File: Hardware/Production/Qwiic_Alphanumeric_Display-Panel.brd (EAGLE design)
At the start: 40.6 x 30.5 mm, 32 parts, among them J1 PTH, J2 Qwiic Right Angle, U2 HT16K33

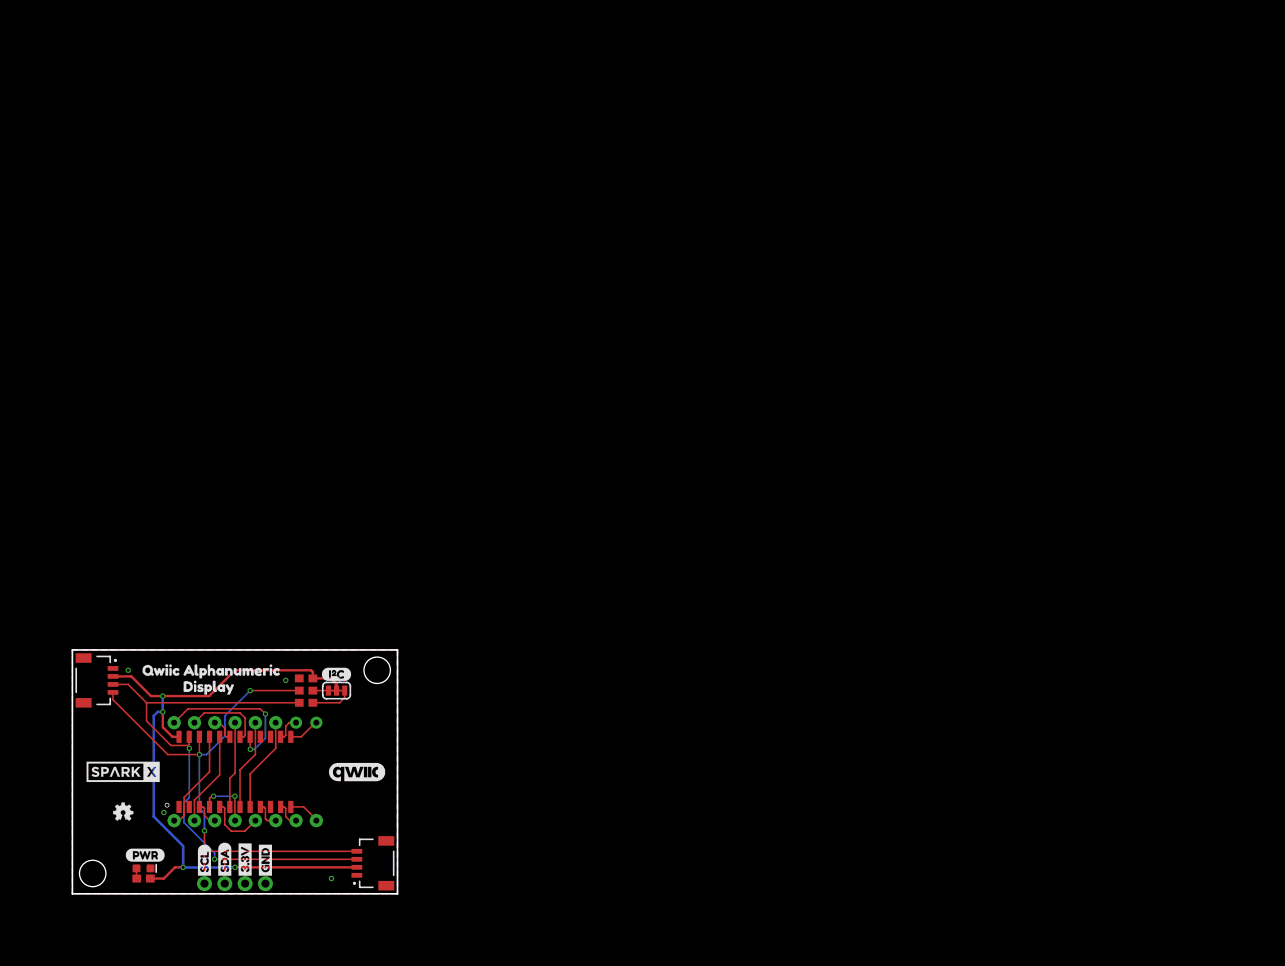
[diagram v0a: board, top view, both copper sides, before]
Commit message: Added Panelized Board and Gerber Files
Updated the HT16K33 Footprint, fixed the board files to match the footprint, added the panelized production board and gerber files for ordering the board
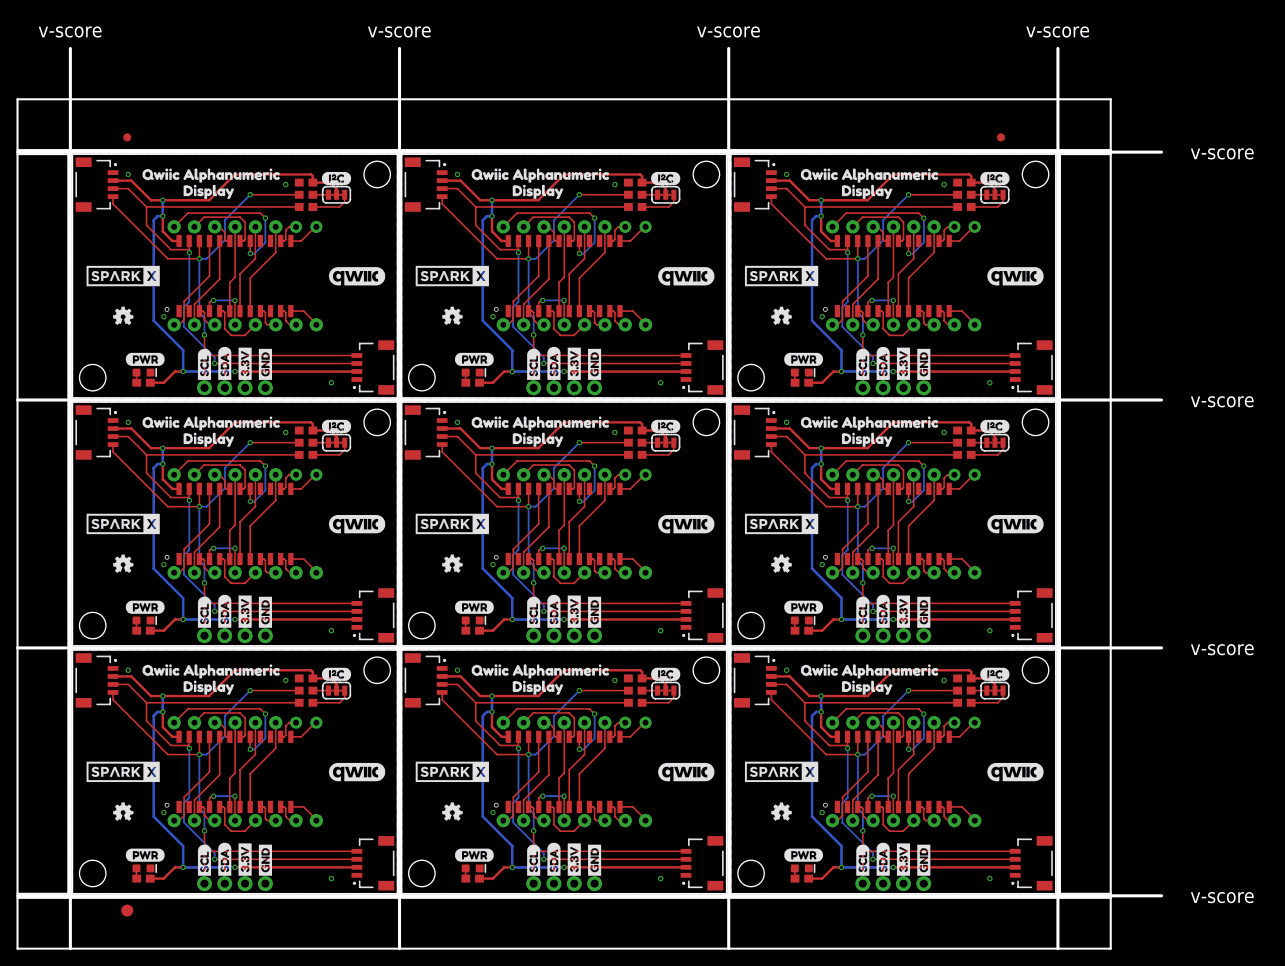
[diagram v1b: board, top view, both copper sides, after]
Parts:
- removed FRAME1: FRAME-LETTER, SparkFun-Aesthetics:CREATIVE_COMMONS
- added C2, C3, C4, C5, C6, C7, C8, C9: 0.1uF, SparkFun-Capacitors:0603
- added D2, D3, D4, D5, D6, D7, D8, D9: RED, SparkFun-LED:LED-0603
- added E$1, E$2: (no value), SparkFun-Aesthetics:FIDUCIAL-1X2
- added E$3: (no value), SparkFun-Retired:FIDUCIAL-1.5X3
- added I2C1, I2C2, I2C3, I2C4, I2C5, I2C6, I2C7, I2C8: JUMPER-SMT_3_2-NC_TRACE_SILK, SparkFun-Jumpers:SMT-JUMPER_3_2-NC_TRACE_SILK
- added J10, J13, J16, J19, J22, J25, J4, J7: PTH, SparkFun-Connectors:JST04_1MM_RA
- added J11, J14, J17, J20, J23, J26, J5, J8: Qwiic Right Angle, SparkFun-Connectors:JST04_1MM_RA
- added J12, J15, J18, J21, J24, J27, J6, J9: (no value), SparkFun-Connectors:1X04_NO_SILK
- added JP10, JP11, JP12, JP13, JP14, JP15, JP16, JP17, JP18, JP2, JP3, JP4, JP5, JP6, JP7, JP9: STAND-OFF, SparkFun:STAND-OFF
- added LOGO2, LOGO3, LOGO4, LOGO5, LOGO6, LOGO7, LOGO8, LOGO9: OSHW-LOGOMINI, SparkFun-Aesthetics:OSHW-LOGO-MINI
- added R10, R13, R16, R19, R2, R22, R25, R7: 1k, SparkFun-Resistors:0603
- added R11, R12, R14, R15, R17, R18, R20, R21, R23, R24, R26, R27, R3, R6, R8, R9: 2.2k, SparkFun-Resistors:0603
- added U$100, U$102, U$117, U$119, U$134, U$136, U$151, U$153, U$32, U$34, U$49, U$51, U$66, U$68, U$83, U$85: (no value), buzzard_labels (4):DISPLAY1
- added U$101, U$116, U$118, U$133, U$135, U$150, U$152, U$31, U$33, U$48, U$50, U$65, U$67, U$82, U$84, U$99: (no value), buzzard_labels (4):QWIIC_ALPHANUMERIC0
- added U$103, U$108, U$120, U$125, U$137, U$142, U$18, U$23, U$35, U$40, U$52, U$57, U$69, U$74, U$86, U$91: (no value), buzzard_labels:3#3V1
- added U$104, U$109, U$121, U$126, U$138, U$143, U$19, U$24, U$36, U$41, U$53, U$58, U$70, U$75, U$87, U$92: (no value), buzzard_labels:GND0
- added U$105, U$122, U$139, U$20, U$37, U$54, U$71, U$88: (no value), buzzard_labels:PWR5
- added U$106, U$110, U$123, U$127, U$140, U$144, U$21, U$25, U$38, U$42, U$55, U$59, U$72, U$76, U$89, U$93: (no value), buzzard_labels:SCL3
- added U$107, U$111, U$124, U$128, U$141, U$145, U$22, U$26, U$39, U$43, U$56, U$60, U$73, U$77, U$90, U$94: (no value), buzzard_labels:SDA2
- added U$112, U$129, U$146, U$27, U$44, U$61, U$78, U$95: (no value), Labels:I_SUPER2_C-()-04
- added U$113, U$130, U$147, U$28, U$45, U$62, U$79, U$96: (no value), Labels:QWIIC_COPYRIGHT_MEDIUM
- added U$114, U$115, U$131, U$132, U$148, U$149, U$29, U$30, U$46, U$47, U$63, U$64, U$80, U$81, U$97, U$98: (no value), SparkX:SPARKX-MEDIUM
- added U10, U12, U14, U16, U18, U4, U6, U8: HT16K33, Alphanumeric_Display_Library:HT16K33
- added U11, U13, U15, U17, U3, U5, U7, U9: (no value), Alphanumeric_Display_Library:SILSMART_DISPLAY
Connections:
- new net 3.3V1: C2.1, I2C1.2, J4.2, J5.2, J6.2, R2.2, U4.24
- new net 3.3V2: C3.1, I2C2.2, J7.2, J8.2, J9.2, R7.2, U6.24
- new net 3.3V3: C4.1, I2C3.2, J10.2, J11.2, J12.2, R10.2, U8.24
- new net 3.3V4: C5.1, I2C4.2, J13.2, J14.2, J15.2, R13.2, U10.24
- new net 3.3V5: C6.1, I2C5.2, J16.2, J17.2, J18.2, R16.2, U12.24
- new net 3.3V6: C7.1, I2C6.2, J19.2, J20.2, J21.2, R19.2, U14.24
- new net 3.3V7: C8.1, I2C7.2, J22.2, J23.2, J24.2, R22.2, U16.24
- new net 3.3V8: C9.1, I2C8.2, J25.2, J26.2, J27.2, R25.2, U18.24
- new net COM_A1: U3.14, U4.8
- new net COM_A2: U5.14, U6.8
- new net COM_A3: U7.14, U8.8
- new net COM_A4: U10.8, U9.14
- new net COM_A5: U11.14, U12.8
- new net COM_A6: U13.14, U14.8
- new net COM_A7: U15.14, U16.8
- new net COM_A8: U17.14, U18.8
- new net COM_B1: U3.13, U4.7
- new net COM_B2: U5.13, U6.7
- new net COM_B3: U7.13, U8.7
- new net COM_B4: U10.7, U9.13
- new net COM_B5: U11.13, U12.7
- new net COM_B6: U13.13, U14.7
- new net COM_B7: U15.13, U16.7
- new net COM_B8: U17.13, U18.7
- new net COM_C1: U3.4, U4.5
- new net COM_C2: U5.4, U6.5
- new net COM_C3: U7.4, U8.5
- new net COM_C4: U10.5, U9.4
- new net COM_C5: U11.4, U12.5
- new net COM_C6: U13.4, U14.5
- new net COM_C7: U15.4, U16.5
- new net COM_C8: U17.4, U18.5
- new net COM_D1: U3.3, U4.9
- new net COM_D2: U5.3, U6.9
- new net COM_D3: U7.3, U8.9
- new net COM_D4: U10.9, U9.3
- new net COM_D5: U11.3, U12.9
- new net COM_D6: U13.3, U14.9
- new net COM_D7: U15.3, U16.9
- new net COM_D8: U17.3, U18.9
- new net COM_E1: U3.6, U4.3
- new net COM_E2: U5.6, U6.3
- new net COM_E3: U7.6, U8.3
- new net COM_E4: U10.3, U9.6
- new net COM_E5: U11.6, U12.3
- new net COM_E6: U13.6, U14.3
- new net COM_E7: U15.6, U16.3
- new net COM_E8: U17.6, U18.3
- new net COM_F1: U3.12, U4.6
- new net COM_F2: U5.12, U6.6
- new net COM_F3: U7.12, U8.6
- new net COM_F4: U10.6, U9.12
- new net COM_F5: U11.12, U12.6
- new net COM_F6: U13.12, U14.6
- new net COM_F7: U15.12, U16.6
- new net COM_F8: U17.12, U18.6
- new net COM_G2: U3.5, U4.4
- new net COM_G3: U5.5, U6.4
- new net COM_G4: U7.5, U8.4
- new net COM_G5: U10.4, U9.5
- new net COM_G6: U11.5, U12.4
- new net COM_G7: U13.5, U14.4
- new net COM_G8: U15.5, U16.4
- new net COM_G9: U17.5, U18.4
- new net DIG_1A1: U3.16, U4.13
- new net DIG_1A2: U5.16, U6.13
- new net DIG_1A3: U7.16, U8.13
- new net DIG_1A4: U10.13, U9.16
- new net DIG_1A5: U11.16, U12.13
- new net DIG_1A6: U13.16, U14.13
- new net DIG_1A7: U15.16, U16.13
- new net DIG_1A8: U17.16, U18.13
- new net DIG_1B1: U3.1, U4.12
- new net DIG_1B2: U5.1, U6.12
- new net DIG_1B3: U7.1, U8.12
- new net DIG_1B4: U10.12, U9.1
- new net DIG_1B5: U11.1, U12.12
- new net DIG_1B6: U13.1, U14.12
- new net DIG_1B7: U15.1, U16.12
- new net DIG_1B8: U17.1, U18.12
- new net DIG_2A1: U3.15, U4.14
- new net DIG_2A2: U5.15, U6.14
- new net DIG_2A3: U7.15, U8.14
- new net DIG_2A4: U10.14, U9.15
- new net DIG_2A5: U11.15, U12.14
- new net DIG_2A6: U13.15, U14.14
- new net DIG_2A7: U15.15, U16.14
- new net DIG_2A8: U17.15, U18.14
- new net DIG_2B1: U3.2, U4.11
- new net DIG_2B2: U5.2, U6.11
- new net DIG_2B3: U7.2, U8.11
- new net DIG_2B4: U10.11, U9.2
- new net DIG_2B5: U11.2, U12.11
- new net DIG_2B6: U13.2, U14.11
- new net DIG_2B7: U15.2, U16.11
- new net DIG_2B8: U17.2, U18.11
- new net DIG_3A1: U3.11, U4.19
- new net DIG_3A2: U5.11, U6.19
- new net DIG_3A3: U7.11, U8.19
- new net DIG_3A4: U10.19, U9.11
- new net DIG_3A5: U11.11, U12.19
- new net DIG_3A6: U13.11, U14.19
- new net DIG_3A7: U15.11, U16.19
- new net DIG_3A8: U17.11, U18.19
- new net DIG_3B1: U3.10, U4.18
- new net DIG_3B2: U5.10, U6.18
- new net DIG_3B3: U7.10, U8.18
- new net DIG_3B4: U10.18, U9.10
- new net DIG_3B5: U11.10, U12.18
- new net DIG_3B6: U13.10, U14.18
- new net DIG_3B7: U15.10, U16.18
- new net DIG_3B8: U17.10, U18.18
- new net DIG_4A1: U3.8, U4.21
- new net DIG_4A2: U5.8, U6.21
- new net DIG_4A3: U7.8, U8.21
- new net DIG_4A4: U10.21, U9.8
- new net DIG_4A5: U11.8, U12.21
- new net DIG_4A6: U13.8, U14.21
- new net DIG_4A7: U15.8, U16.21
- new net DIG_4A8: U17.8, U18.21
- new net DIG_4B1: U3.9, U4.17
- new net DIG_4B2: U5.9, U6.17
- new net DIG_4B3: U7.9, U8.17
- new net DIG_4B4: U10.17, U9.9
- new net DIG_4B5: U11.9, U12.17
- new net DIG_4B6: U13.9, U14.17
- new net DIG_4B7: U15.9, U16.17
- new net DIG_4B8: U17.9, U18.17
- new net DIG_DP1: U3.7, U4.20
- new net DIG_DP2: U5.7, U6.20
- new net DIG_DP3: U7.7, U8.20
- new net DIG_DP4: U10.20, U9.7
- new net DIG_DP5: U11.7, U12.20
- new net DIG_DP6: U13.7, U14.20
- new net DIG_DP7: U15.7, U16.20
- new net DIG_DP8: U17.7, U18.20
- new net GND1: C2.2, D2.C, J4.1, J5.1, J6.1, U4.1
- new net GND2: C3.2, D3.C, J7.1, J8.1, J9.1, U6.1
- new net GND3: C4.2, D4.C, J10.1, J11.1, J12.1, U8.1
- new net GND4: C5.2, D5.C, J13.1, J14.1, J15.1, U10.1
- new net GND5: C6.2, D6.C, J16.1, J17.1, J18.1, U12.1
- new net GND6: C7.2, D7.C, J19.1, J20.1, J21.1, U14.1
- new net GND7: C8.2, D8.C, J22.1, J23.1, J24.1, U16.1
- new net GND8: C9.2, D9.C, J25.1, J26.1, J27.1, U18.1
- new net N$10: D4.A, R10.1
- new net N$11: I2C3.1, R12.2
- new net N$12: I2C3.3, R11.2
- new net N$13: D5.A, R13.1
- new net N$14: I2C4.1, R15.2
- new net N$15: I2C4.3, R14.2
- new net N$16: D6.A, R16.1
- new net N$17: I2C5.1, R18.2
- new net N$18: I2C5.3, R17.2
- new net N$19: D7.A, R19.1
- new net N$2: D2.A, R2.1
- new net N$20: I2C6.1, R21.2
- new net N$21: I2C6.3, R20.2
- new net N$22: D8.A, R22.1
- new net N$23: I2C7.1, R24.2
- new net N$24: I2C7.3, R23.2
- new net N$25: D9.A, R25.1
- new net N$26: I2C8.1, R27.2
- new net N$27: I2C8.3, R26.2
- new net N$3: I2C1.1, R6.2
- new net N$6: I2C1.3, R3.2
- new net N$7: D3.A, R7.1
- new net N$8: I2C2.1, R9.2
- new net N$9: I2C2.3, R8.2
- new net SCL1: J4.4, J5.4, J6.4, R6.1, U4.22
- new net SCL2: J7.4, J8.4, J9.4, R9.1, U6.22
- new net SCL3: J10.4, J11.4, J12.4, R12.1, U8.22
- new net SCL4: J13.4, J14.4, J15.4, R15.1, U10.22
- new net SCL5: J16.4, J17.4, J18.4, R18.1, U12.22
- new net SCL6: J19.4, J20.4, J21.4, R21.1, U14.22
- new net SCL7: J22.4, J23.4, J24.4, R24.1, U16.22
- new net SCL8: J25.4, J26.4, J27.4, R27.1, U18.22
- new net SDA1: J4.3, J5.3, J6.3, R3.1, U4.23
- new net SDA2: J7.3, J8.3, J9.3, R8.1, U6.23
- new net SDA3: J10.3, J11.3, J12.3, R11.1, U8.23
- new net SDA4: J13.3, J14.3, J15.3, R14.1, U10.23
- new net SDA5: J16.3, J17.3, J18.3, R17.1, U12.23
- new net SDA6: J19.3, J20.3, J21.3, R20.1, U14.23
- new net SDA7: J22.3, J23.3, J24.3, R23.1, U16.23
- new net SDA8: J25.3, J26.3, J27.3, R26.1, U18.23
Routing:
- net 3.3V6: track 0.00 -> 88.9 mm, vias 0 -> 4
- net 3.3V3: track 0.00 -> 88.9 mm, vias 0 -> 4
- net 3.3V8: track 0.00 -> 88.9 mm, vias 0 -> 4
- net 3.3V7: track 0.00 -> 88.9 mm, vias 0 -> 4
- net 3.3V5: track 0.00 -> 88.9 mm, vias 0 -> 4
- net 3.3V4: track 0.00 -> 88.9 mm, vias 0 -> 4
- net 3.3V2: track 0.00 -> 88.9 mm, vias 0 -> 4
- net 3.3V1: track 0.00 -> 88.9 mm, vias 0 -> 4
- net SDA8: track 0.00 -> 71.1 mm, vias 0 -> 2
- net SDA2: track 0.00 -> 71.1 mm, vias 0 -> 2
- net SDA1: track 0.00 -> 71.1 mm, vias 0 -> 2
- net SDA7: track 0.00 -> 71.1 mm, vias 0 -> 2
- net SDA6: track 0.00 -> 71.1 mm, vias 0 -> 2
- net SDA5: track 0.00 -> 71.1 mm, vias 0 -> 2
- net SDA4: track 0.00 -> 71.1 mm, vias 0 -> 2
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- added copper zone on layer 1, net GND1
- added copper zone on layer 16, net GND1
- added copper zone on layer 1, net GND2
- added copper zone on layer 16, net GND2
- added copper zone on layer 1, net GND3
- added copper zone on layer 16, net GND3
- added copper zone on layer 1, net GND4
- added copper zone on layer 16, net GND4
- added copper zone on layer 1, net GND5
- added copper zone on layer 16, net GND5
- added copper zone on layer 1, net GND6
- added copper zone on layer 16, net GND6
- added copper zone on layer 1, net GND7
- added copper zone on layer 16, net GND7
- added copper zone on layer 1, net GND8
- added copper zone on layer 16, net GND8
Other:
- board size 40.6 x 30.5 mm -> 143 x 112.5 mm
- board text added: "v-score"
- board text removed: "I2C"
- board text removed: "Madison Chodikov"
- board text removed: "U1"

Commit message: Rev X02 ordered!
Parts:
- added 3V1, 3V10, 3V11, 3V12, 3V13, 3V14, 3V15, 3V16, 3V17, 3V18, 3V19, 3V2, 3V20, 3V21, 3V22, 3V23, 3V24, 3V25, 3V3, 3V4, 3V5, 3V6, 3V7, 3V8, 3V9: JUMPER-SMT_2_NC_TRACE_SILK, SparkFun-Jumpers:SMT-JUMPER_2_NC_TRACE_SILK
- added C10, C11, C12, C13, C14, C15, C16, C17, C18, C19, C20, C21, C22, C23, C24, C25: 0.1uF, SparkFun-Capacitors:0603
- added D10, D12, D14, D16, D18, D20, D22, D24, D26, D28, D30, D32, D34, D36, D38, D40, D42, D44, D46, D48, D50: 250mA/100V, SparkFun-DiscreteSemi:SOD-323
- added D11, D13, D15, D17, D19, D21, D23, D25, D27, D29, D31, D33, D35, D37, D39, D41, D43, D45, D47, D49: RED, SparkFun-LED:LED-0603
- added FD1, FD10, FD100, FD11, FD12, FD13, FD14, FD15, FD16, FD17, FD18, FD19, FD2, FD20, FD21, FD22, FD23, FD24, FD25, FD26, FD27, FD28, FD29, FD3, FD30, FD31, FD32, FD33, FD34, FD35, FD36, FD37, FD38, FD39, FD4, FD40, FD41, FD42, FD43, FD44, FD45, FD46, FD47, FD48, FD49, FD5, FD50, FD51, FD52, FD53, FD54, FD55, FD56, FD57, FD58, FD59, FD6, FD60, FD61, FD62, FD63, FD64, FD65, FD66, FD67, FD68, FD69, FD7, FD70, FD71, FD72, FD73, FD74, FD75, FD76, FD77, FD78, FD79, FD8, FD80, FD81, FD82, FD83, FD84, FD85, FD86, FD87, FD88, FD89, FD9, FD90, FD91, FD92, FD93, FD94, FD95, FD96, FD97, FD98, FD99: FIDUCIAL1X2, SparkFun-Aesthetics:FIDUCIAL-1X2
- added H1, H10, H100, H11, H12, H13, H14, H15, H16, H17, H18, H19, H2, H20, H21, H22, H23, H24, H25, H26, H27, H28, H29, H3, H30, H31, H32, H33, H34, H35, H36, H37, H38, H39, H4, H40, H41, H42, H43, H44, H45, H46, H47, H48, H49, H5, H50, H51, H52, H53, H54, H55, H56, H57, H58, H59, H6, H60, H61, H62, H63, H64, H65, H66, H67, H68, H69, H7, H70, H71, H72, H73, H74, H75, H76, H77, H78, H79, H8, H80, H81, H82, H83, H84, H85, H86, H87, H88, H89, H9, H90, H91, H92, H93, H94, H95, H96, H97, H98, H99: STAND-OFF, SparkFun-Hardware:STAND-OFF
- added I2C10, I2C11, I2C12, I2C13, I2C14, I2C15, I2C16, I2C17, I2C18, I2C19, I2C20, I2C21, I2C22, I2C23, I2C24, I2C9: JUMPER-SMT_3_2-NC_TRACE_SILK, SparkFun-Jumpers:SMT-JUMPER_3_2-NC_TRACE_SILK
- added IC1, IC10, IC11, IC12, IC13, IC14, IC15, IC16, IC17, IC18, IC19, IC2, IC20, IC21, IC22, IC23, IC24, IC25, IC3, IC4, IC5, IC6, IC7, IC8, IC9: (no value), Alphanumeric_Display_Library:HT16K33
- added J28, J31, J34, J37, J40, J43, J46, J49, J52, J55, J58, J61, J64, J67, J70, J73: (no value), SparkFun-Connectors:1X04_NO_SILK
- added J29, J30, J32, J33, J35, J36, J38, J39, J41, J42, J44, J45, J47, J48, J50, J51, J53, J54, J56, J57, J59, J60, J62, J63, J65, J66, J68, J69, J71, J72, J74, J75: Vertical Qwiic Connector, SparkFun-Connectors:JST04_1MM_VERT
- added JP19, JP20, JP21, JP22, JP23, JP24, JP25, JP26, JP27, JP28, JP29, JP30, JP31, JP32, JP33, JP34, JP35, JP36, JP37, JP38, JP39, JP40, JP41, JP42, JP43, JP44, JP45, JP46, JP47, JP48, JP49, JP50: JUMPER-SMT_2_NO_SILK, SparkFun-Jumpers:SMT-JUMPER_2_NO_SILK
- added LOGO10, LOGO11, LOGO12, LOGO13, LOGO14, LOGO15, LOGO16, LOGO17, LOGO18, LOGO19, LOGO20, LOGO21, LOGO22, LOGO23, LOGO24, LOGO25: OSHW-LOGOMINI, SparkFun-Aesthetics:OSHW-LOGO-MINI
- added R100, R104, R105, R109, R110, R114, R115, R119, R120, R124, R125, R29, R30, R34, R35, R39, R40, R44, R45, R49, R50, R54, R55, R59, R60, R64, R65, R69, R70, R74, R75, R79, R80, R84, R85, R89, R90, R94, R95, R99: 39k, SparkFun-Resistors:0603
- added R101, R106, R111, R116, R121, R31, R36, R41, R46, R51, R56, R61, R66, R71, R76, R81, R86, R91, R96: 1k, SparkFun-Resistors:0603
- added R102, R103, R107, R108, R112, R113, R117, R118, R122, R123, R28, R32, R33, R37, R38, R42, R43, R47, R48, R52, R53, R57, R58, R62, R63, R67, R68, R72, R73, R77, R78, R82, R83, R87, R88, R92, R93, R97, R98: 2.2k, SparkFun-Resistors:0603
- added U$154, U$171, U$188, U$205, U$222, U$239, U$256, U$273, U$290, U$307, U$324, U$341, U$358, U$375, U$392, U$409: (no value), buzzard_labels:PWR5
- added U$155, U$172, U$189, U$206, U$223, U$240, U$257, U$274, U$291, U$308, U$325, U$342, U$359, U$376, U$393, U$410: (no value), Labels:I_SUPER2_C-()-04
- added U$156, U$158, U$173, U$175, U$190, U$192, U$207, U$209, U$224, U$226, U$241, U$243, U$258, U$260, U$275, U$277, U$292, U$294, U$309, U$311, U$326, U$328, U$343, U$345, U$360, U$362, U$377, U$379, U$394, U$396, U$411, U$413: (no value), buzzard_labels (4):QWIIC_ALPHANUMERIC0
- added U$157, U$159, U$174, U$176, U$191, U$193, U$208, U$210, U$225, U$227, U$242, U$244, U$259, U$261, U$276, U$278, U$293, U$295, U$310, U$312, U$327, U$329, U$344, U$346, U$361, U$363, U$378, U$380, U$395, U$397, U$412, U$414: (no value), buzzard_labels (4):DISPLAY1
- added U$160, U$161, U$177, U$178, U$194, U$195, U$211, U$212, U$228, U$229, U$245, U$246, U$262, U$263, U$279, U$280, U$296, U$297, U$313, U$314, U$330, U$331, U$347, U$348, U$364, U$365, U$381, U$382, U$398, U$399, U$415, U$416: MOUNTING_HOLE_M2-0.4X6, Alphanumeric_Display_Library:MOUNTING_HOLE_M2-0.4X6
- added U$162, U$179, U$196, U$213, U$230, U$247, U$264, U$281, U$298, U$315, U$332, U$349, U$366, U$383, U$400, U$417: (no value), buzzard_labels (63):A00
- added U$163, U$180, U$197, U$214, U$231, U$248, U$265, U$282, U$299, U$316, U$333, U$350, U$367, U$384, U$401, U$418: (no value), buzzard_labels (63):A11
- added U$164, U$181, U$198, U$215, U$232, U$249, U$266, U$283, U$300, U$317, U$334, U$351, U$368, U$385, U$402, U$419: (no value), SparkFun-Aesthetics:QWIIC_4MM
- added U$165, U$182, U$199, U$216, U$233, U$250, U$267, U$284, U$301, U$318, U$335, U$352, U$369, U$386, U$403, U$420: (no value), buzzard_labels (65):32
- added U$166, U$183, U$200, U$217, U$234, U$251, U$268, U$285, U$302, U$319, U$336, U$353, U$370, U$387, U$404, U$421: (no value), buzzard_labels (65):C0
- added U$167, U$184, U$201, U$218, U$235, U$252, U$269, U$286, U$303, U$320, U$337, U$354, U$371, U$388, U$405, U$422: (no value), buzzard_labels (65):D1
- added U$168, U$185, U$202, U$219, U$236, U$253, U$270, U$287, U$304, U$321, U$338, U$355, U$372, U$389, U$406, U$423: (no value), buzzard_labels (65):G3
- added U$169, U$170, U$186, U$187, U$203, U$204, U$220, U$221, U$237, U$238, U$254, U$255, U$271, U$272, U$288, U$289, U$305, U$306, U$322, U$323, U$339, U$340, U$356, U$357, U$373, U$374, U$390, U$391, U$407, U$408, U$424, U$425: SPARKX-LOGO4, SparkX:SPARKX-MEDIUM
- added U19, U20, U21, U22, U23, U24, U25: (no value), Alphanumeric_Display_Library:SILSMART_DISPLAY
- D2, D4, D6, D8: value RED -> 250mA/100V; device SparkFun-LED:LED-0603 -> SparkFun-DiscreteSemi:SOD-323
- J1, J10, J13, J16, J19, J22, J25, J7: value PTH -> (none); device SparkFun-Connectors:JST04_1MM_RA -> SparkFun-Connectors:1X04_NO_SILK
- J11, J14, J17, J2, J20, J23, J26, J5, J8: value Qwiic Right Angle -> Vertical Qwiic Connector; device SparkFun-Connectors:JST04_1MM_RA -> SparkFun-Connectors:JST04_1MM_VERT
- J12, J15, J18, J21, J24, J27, J6, J9: value (none) -> Vertical Qwiic Connector; device SparkFun-Connectors:1X04_NO_SILK -> SparkFun-Connectors:JST04_1MM_VERT
- J4: value PTH -> Vertical Qwiic Connector; device SparkFun-Connectors:JST04_1MM_RA -> SparkFun-Connectors:JST04_1MM_VERT
- JP1, JP10, JP11, JP12, JP13, JP14, JP15, JP16, JP17, JP18, JP2, JP3, JP4, JP5, JP6, JP7, JP8, JP9: value STAND-OFF -> JUMPER-SMT_2_NO_SILK; device SparkFun:STAND-OFF -> SparkFun-Jumpers:SMT-JUMPER_2_NO_SILK
- R10, R19, R2, R25: value 1k -> 39k
- R11, R21, R26, R6: value 2.2k -> 1k
- R13, R22, R7: value 1k -> 2.2k
- R14, R15, R20, R24, R3, R9: value 2.2k -> 39k
- U$1: device buzzard_labels:3#3V1 -> buzzard_labels (65):32
- U$100, U$117, U$134, U$151, U$32, U$49, U$66, U$83: device buzzard_labels (4):DISPLAY1 -> buzzard_labels (65):G3
- U$101, U$118, U$135, U$152, U$33, U$50, U$67, U$84: value (none) -> SPARKX-LOGO4; device buzzard_labels (4):QWIIC_ALPHANUMERIC0 -> SparkX:SPARKX-MEDIUM
- U$102, U$119, U$136, U$153, U$34, U$51, U$68, U$85: value (none) -> SPARKX-LOGO4; device buzzard_labels (4):DISPLAY1 -> SparkX:SPARKX-MEDIUM
- U$103, U$120, U$137, U$35, U$52, U$69, U$86: device buzzard_labels:3#3V1 -> buzzard_labels:PWR5
- U$104, U$121, U$138, U$36, U$53, U$70, U$87: device buzzard_labels:GND0 -> Labels:I_SUPER2_C-()-04
- U$105, U$122, U$139, U$37, U$54, U$71, U$88: device buzzard_labels:PWR5 -> buzzard_labels (4):QWIIC_ALPHANUMERIC0
- U$106, U$123, U$140, U$38, U$55, U$72, U$89: device buzzard_labels:SCL3 -> buzzard_labels (4):DISPLAY1
- U$107, U$124, U$141, U$22, U$39, U$56, U$73, U$90: device buzzard_labels:SDA2 -> buzzard_labels (4):QWIIC_ALPHANUMERIC0
- U$108, U$125, U$142, U$23, U$40, U$57, U$74, U$91: device buzzard_labels:3#3V1 -> buzzard_labels (4):DISPLAY1
- U$109, U$126, U$143, U$19, U$24, U$41, U$58, U$75, U$92: value (none) -> MOUNTING_HOLE_M2-0.4X6; device buzzard_labels:GND0 -> Alphanumeric_Display_Library:MOUNTING_HOLE_M2-0.4X6
- U$11: device Labels:QWIIC_COPYRIGHT_MEDIUM -> Labels:I_SUPER2_C-()-04
- U$110, U$127, U$144, U$25, U$42, U$59, U$76, U$93: value (none) -> MOUNTING_HOLE_M2-0.4X6; device buzzard_labels:SCL3 -> Alphanumeric_Display_Library:MOUNTING_HOLE_M2-0.4X6
- U$111, U$128, U$145, U$26, U$43, U$60, U$77, U$94: device buzzard_labels:SDA2 -> buzzard_labels (63):A00
- U$112, U$129, U$146, U$27, U$44, U$61, U$78, U$95: device Labels:I_SUPER2_C-()-04 -> buzzard_labels (63):A11
- U$113, U$130, U$147, U$28, U$45, U$62, U$79, U$96: device Labels:QWIIC_COPYRIGHT_MEDIUM -> SparkFun-Aesthetics:QWIIC_4MM
- U$114, U$131, U$148, U$29, U$46, U$63, U$80, U$97: device SparkX:SPARKX-MEDIUM -> buzzard_labels (65):32
- U$115, U$132, U$149, U$30, U$47, U$64, U$81, U$98: device SparkX:SPARKX-MEDIUM -> buzzard_labels (65):C0
- U$116, U$133, U$150, U$31, U$48, U$65, U$82, U$99: device buzzard_labels (4):QWIIC_ALPHANUMERIC0 -> buzzard_labels (65):D1
- U$12: device SparkX:SPARKX-MEDIUM -> buzzard_labels (4):QWIIC_ALPHANUMERIC0
- U$14: device SparkX:SPARKX-MEDIUM -> buzzard_labels (4):DISPLAY1
- U$18: value (none) -> MOUNTING_HOLE_M2-0.4X6; device buzzard_labels:3#3V1 -> Alphanumeric_Display_Library:MOUNTING_HOLE_M2-0.4X6
- U$2: device buzzard_labels:GND0 -> buzzard_labels (65):C0
- U$20: device buzzard_labels:PWR5 -> buzzard_labels (63):A00
- U$21: device buzzard_labels:SCL3 -> buzzard_labels (63):A11
- U$4: device buzzard_labels:SCL3 -> buzzard_labels (65):D1
- U$5: device buzzard_labels:SDA2 -> buzzard_labels (65):G3
- U$6: device buzzard_labels:3#3V1 -> SparkFun-Aesthetics:QWIIC_4MM
- U$7: value (none) -> SPARKX-LOGO4; device buzzard_labels:GND0 -> SparkX:SPARKX-MEDIUM
- U$8: value (none) -> SPARKX-LOGO4; device buzzard_labels:SCL3 -> SparkX:SPARKX-MEDIUM
- U$9: device buzzard_labels:SDA2 -> buzzard_labels:PWR5
- U10, U12, U14, U16, U18, U2, U4, U6, U8: value HT16K33 -> (none); device Alphanumeric_Display_Library:HT16K33 -> Alphanumeric_Display_Library:SILSMART_DISPLAY
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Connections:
- new net 3.3V10: 3V11.2, C11.1, I2C10.2, IC11.24, J31.2, J32.2, J33.2
- new net 3.3V11: 3V12.2, C12.1, I2C11.2, IC12.24, J34.2, J35.2, J36.2
- new net 3.3V12: 3V13.2, C13.1, I2C12.2, IC13.24, J37.2, J38.2, J39.2
- new net 3.3V13: 3V14.2, C14.1, I2C13.2, IC14.24, J40.2, J41.2, J42.2
- new net 3.3V14: 3V15.2, C15.1, I2C14.2, IC15.24, J43.2, J44.2, J45.2
- new net 3.3V15: 3V16.2, C16.1, I2C15.2, IC16.24, J46.2, J47.2, J48.2
- new net 3.3V16: 3V17.2, C17.1, I2C16.2, IC17.24, J49.2, J50.2, J51.2
- new net 3.3V17: 3V18.2, C18.1, I2C17.2, IC18.24, J52.2, J53.2, J54.2
- new net 3.3V18: 3V19.2, C19.1, I2C18.2, IC19.24, J55.2, J56.2, J57.2
- new net 3.3V19: 3V20.2, C20.1, I2C19.2, IC20.24, J58.2, J59.2, J60.2
- new net 3.3V20: 3V21.2, C21.1, I2C20.2, IC21.24, J61.2, J62.2, J63.2
- new net 3.3V21: 3V22.2, C22.1, I2C21.2, IC22.24, J64.2, J65.2, J66.2
- new net 3.3V22: 3V23.2, C23.1, I2C22.2, IC23.24, J67.2, J68.2, J69.2
- new net 3.3V23: 3V24.2, C24.1, I2C23.2, IC24.24, J70.2, J71.2, J72.2
- new net 3.3V24: 3V25.2, C25.1, I2C24.2, IC25.24, J73.2, J74.2, J75.2
- new net 3.3V9: 3V10.2, C10.1, I2C9.2, IC10.24, J28.2, J29.2, J30.2
- new net COM_A10: D22.A, IC11.2, U11.14
- new net COM_A11: D24.A, IC12.2, U12.14
- new net COM_A12: D26.A, IC13.2, U13.14
- new net COM_A13: D28.A, IC14.2, U14.14
- new net COM_A14: D30.A, IC15.2, U15.14
- new net COM_A15: D32.A, IC16.2, U16.14
- new net COM_A16: D34.A, IC17.2, U17.14
- new net COM_A17: D36.A, IC18.2, U18.14
- new net COM_A18: D38.A, IC19.2, U19.14
- new net COM_A19: D40.A, IC20.2, U20.14
- new net COM_A20: D42.A, IC21.2, U21.14
- new net COM_A21: D44.A, IC22.2, U22.14
- new net COM_A22: D46.A, IC23.2, U23.14
- new net COM_A23: D48.A, IC24.2, U24.14
- new net COM_A24: D50.A, IC25.2, U25.14
- new net COM_A9: D20.A, IC10.2, U10.14
- new net COM_B10: IC11.3, U11.13
- new net COM_B11: IC12.3, U12.13
- new net COM_B12: IC13.3, U13.13
- new net COM_B13: IC14.3, U14.13
- new net COM_B14: IC15.3, U15.13
- new net COM_B15: IC16.3, U16.13
- new net COM_B16: IC17.3, U17.13
- new net COM_B17: IC18.3, U18.13
- new net COM_B18: IC19.3, U19.13
- new net COM_B19: IC20.3, U20.13
- new net COM_B20: IC21.3, U21.13
- new net COM_B21: IC22.3, U22.13
- new net COM_B22: IC23.3, U23.13
- new net COM_B23: IC24.3, U24.13
- new net COM_B24: IC25.3, U25.13
- new net COM_B9: IC10.3, U10.13
- new net COM_C10: IC11.4, U11.4
- new net COM_C11: IC12.4, U12.4
- new net COM_C12: IC13.4, U13.4
- new net COM_C13: IC14.4, U14.4
- new net COM_C14: IC15.4, U15.4
- new net COM_C15: IC16.4, U16.4
- new net COM_C16: IC17.4, U17.4
- new net COM_C17: IC18.4, U18.4
- new net COM_C18: IC19.4, U19.4
- new net COM_C19: IC20.4, U20.4
- new net COM_C20: IC21.4, U21.4
- new net COM_C21: IC22.4, U22.4
- new net COM_C22: IC23.4, U23.4
- new net COM_C23: IC24.4, U24.4
- new net COM_C24: IC25.4, U25.4
- new net COM_C9: IC10.4, U10.4
- new net COM_D10: IC11.5, U11.3
- new net COM_D11: IC12.5, U12.3
- new net COM_D12: IC13.5, U13.3
- new net COM_D13: IC14.5, U14.3
- new net COM_D14: IC15.5, U15.3
- new net COM_D15: IC16.5, U16.3
- new net COM_D16: IC17.5, U17.3
- new net COM_D17: IC18.5, U18.3
- new net COM_D18: IC19.5, U19.3
- new net COM_D19: IC20.5, U20.3
- new net COM_D20: IC21.5, U21.3
- new net COM_D21: IC22.5, U22.3
- new net COM_D22: IC23.5, U23.3
- new net COM_D23: IC24.5, U24.3
- new net COM_D24: IC25.5, U25.3
- new net COM_D9: IC10.5, U10.3
- new net COM_E10: IC11.6, U11.6
- new net COM_E11: IC12.6, U12.6
- new net COM_E12: IC13.6, U13.6
- new net COM_E13: IC14.6, U14.6
- new net COM_E14: IC15.6, U15.6
- new net COM_E15: IC16.6, U16.6
- new net COM_E16: IC17.6, U17.6
- new net COM_E17: IC18.6, U18.6
- new net COM_E18: IC19.6, U19.6
- new net COM_E19: IC20.6, U20.6
- new net COM_E20: IC21.6, U21.6
- new net COM_E21: IC22.6, U22.6
- new net COM_E22: IC23.6, U23.6
- new net COM_E23: IC24.6, U24.6
- new net COM_E24: IC25.6, U25.6
- new net COM_E9: IC10.6, U10.6
- new net COM_F10: IC11.7, U11.12
- new net COM_F11: IC12.7, U12.12
- new net COM_F12: IC13.7, U13.12
- new net COM_F13: IC14.7, U14.12
- new net COM_F14: IC15.7, U15.12
- new net COM_F15: IC16.7, U16.12
- new net COM_F16: IC17.7, U17.12
- new net COM_F17: IC18.7, U18.12
- new net COM_F18: IC19.7, U19.12
- new net COM_F19: IC20.7, U20.12
- new net COM_F20: IC21.7, U21.12
- new net COM_F21: IC22.7, U22.12
- new net COM_F22: IC23.7, U23.12
- new net COM_F23: IC24.7, U24.12
- new net COM_F24: IC25.7, U25.12
- new net COM_F9: IC10.7, U10.12
- new net COM_G: IC1.8, U1.5
- new net COM_G10: IC11.8, U11.5
- new net COM_G11: IC12.8, U12.5
- new net COM_G12: IC13.8, U13.5
- new net COM_G13: IC14.8, U14.5
- new net COM_G14: IC15.8, U15.5
- new net COM_G15: IC16.8, U16.5
- new net COM_G16: IC17.8, U17.5
- new net COM_G17: IC18.8, U18.5
- new net COM_G18: IC19.8, U19.5
- new net COM_G19: IC20.8, U20.5
- new net COM_G20: IC21.8, U21.5
- new net COM_G21: IC22.8, U22.5
- new net COM_G22: IC23.8, U23.5
- new net COM_G23: IC24.8, U24.5
- new net COM_G24: IC25.8, U25.5
- new net DIG_1A10: IC11.21, JP21.1, U11.16
- new net DIG_1A11: IC12.21, JP23.1, U12.16
- new net DIG_1A12: IC13.21, JP25.1, U13.16
- new net DIG_1A13: IC14.21, JP27.1, U14.16
- new net DIG_1A14: IC15.21, JP29.1, U15.16
- new net DIG_1A15: IC16.21, JP31.1, U16.16
- new net DIG_1A16: IC17.21, JP33.1, U17.16
- new net DIG_1A17: IC18.21, JP35.1, U18.16
- new net DIG_1A18: IC19.21, JP37.1, U19.16
- new net DIG_1A19: IC20.21, JP39.1, U20.16
- new net DIG_1A20: IC21.21, JP41.1, U21.16
- new net DIG_1A21: IC22.21, JP43.1, U22.16
- new net DIG_1A22: IC23.21, JP45.1, U23.16
- new net DIG_1A23: IC24.21, JP47.1, U24.16
- new net DIG_1A24: IC25.21, JP49.1, U25.16
- new net DIG_1A9: IC10.21, JP19.1, U10.16
- new net DIG_1B10: IC11.17, U11.1
- new net DIG_1B11: IC12.17, U12.1
- new net DIG_1B12: IC13.17, U13.1
- new net DIG_1B13: IC14.17, U14.1
- new net DIG_1B14: IC15.17, U15.1
- new net DIG_1B15: IC16.17, U16.1
- new net DIG_1B16: IC17.17, U17.1
- new net DIG_1B17: IC18.17, U18.1
- new net DIG_1B18: IC19.17, U19.1
- new net DIG_1B19: IC20.17, U20.1
- new net DIG_1B20: IC21.17, U21.1
- new net DIG_1B21: IC22.17, U22.1
- new net DIG_1B22: IC23.17, U23.1
- new net DIG_1B23: IC24.17, U24.1
- new net DIG_1B24: IC25.17, U25.1
- new net DIG_1B9: IC10.17, U10.1
- new net DIG_2A10: IC11.20, JP22.1, U11.15
- new net DIG_2A11: IC12.20, JP24.1, U12.15
- new net DIG_2A12: IC13.20, JP26.1, U13.15
- new net DIG_2A13: IC14.20, JP28.1, U14.15
- new net DIG_2A14: IC15.20, JP30.1, U15.15
- new net DIG_2A15: IC16.20, JP32.1, U16.15
- new net DIG_2A16: IC17.20, JP34.1, U17.15
- new net DIG_2A17: IC18.20, JP36.1, U18.15
- new net DIG_2A18: IC19.20, JP38.1, U19.15
- new net DIG_2A19: IC20.20, JP40.1, U20.15
- new net DIG_2A20: IC21.20, JP42.1, U21.15
- new net DIG_2A21: IC22.20, JP44.1, U22.15
- new net DIG_2A22: IC23.20, JP46.1, U23.15
- new net DIG_2A23: IC24.20, JP48.1, U24.15
- new net DIG_2A24: IC25.20, JP50.1, U25.15
- new net DIG_2A9: IC10.20, JP20.1, U10.15
- new net DIG_2B10: IC11.16, U11.2
- new net DIG_2B11: IC12.16, U12.2
- new net DIG_2B12: IC13.16, U13.2
- new net DIG_2B13: IC14.16, U14.2
- new net DIG_2B14: IC15.16, U15.2
- new net DIG_2B15: IC16.16, U16.2
- new net DIG_2B16: IC17.16, U17.2
- new net DIG_2B17: IC18.16, U18.2
- new net DIG_2B18: IC19.16, U19.2
- new net DIG_2B19: IC20.16, U20.2
- new net DIG_2B20: IC21.16, U21.2
- new net DIG_2B21: IC22.16, U22.2
- new net DIG_2B22: IC23.16, U23.2
- new net DIG_2B23: IC24.16, U24.2
- new net DIG_2B24: IC25.16, U25.2
- new net DIG_2B9: IC10.16, U10.2
- new net DIG_3A10: IC11.19, U11.11
- new net DIG_3A11: IC12.19, U12.11
- new net DIG_3A12: IC13.19, U13.11
- new net DIG_3A13: IC14.19, U14.11
- new net DIG_3A14: IC15.19, U15.11
- new net DIG_3A15: IC16.19, U16.11
- new net DIG_3A16: IC17.19, U17.11
- new net DIG_3A17: IC18.19, U18.11
- new net DIG_3A18: IC19.19, U19.11
- new net DIG_3A19: IC20.19, U20.11
- new net DIG_3A20: IC21.19, U21.11
- new net DIG_3A21: IC22.19, U22.11
- new net DIG_3A22: IC23.19, U23.11
- new net DIG_3A23: IC24.19, U24.11
- new net DIG_3A24: IC25.19, U25.11
- new net DIG_3A9: IC10.19, U10.11
- new net DIG_3B10: IC11.15, U11.10
- new net DIG_3B11: IC12.15, U12.10
- new net DIG_3B12: IC13.15, U13.10
- new net DIG_3B13: IC14.15, U14.10
- new net DIG_3B14: IC15.15, U15.10
- new net DIG_3B15: IC16.15, U16.10
- new net DIG_3B16: IC17.15, U17.10
- new net DIG_3B17: IC18.15, U18.10
- new net DIG_3B18: IC19.15, U19.10
- new net DIG_3B19: IC20.15, U20.10
- new net DIG_3B20: IC21.15, U21.10
- new net DIG_3B21: IC22.15, U22.10
- new net DIG_3B22: IC23.15, U23.10
- new net DIG_3B23: IC24.15, U24.10
- new net DIG_3B24: IC25.15, U25.10
- new net DIG_3B9: IC10.15, U10.10
- new net DIG_4A10: IC11.18, U11.8
- new net DIG_4A11: IC12.18, U12.8
- new net DIG_4A12: IC13.18, U13.8
- new net DIG_4A13: IC14.18, U14.8
- new net DIG_4A14: IC15.18, U15.8
- new net DIG_4A15: IC16.18, U16.8
- new net DIG_4A16: IC17.18, U17.8
- new net DIG_4A17: IC18.18, U18.8
- new net DIG_4A18: IC19.18, U19.8
- new net DIG_4A19: IC20.18, U20.8
- new net DIG_4A20: IC21.18, U21.8
- new net DIG_4A21: IC22.18, U22.8
- new net DIG_4A22: IC23.18, U23.8
- new net DIG_4A23: IC24.18, U24.8
- new net DIG_4A24: IC25.18, U25.8
- new net DIG_4A9: IC10.18, U10.8
- new net DIG_4B10: IC11.14, U11.9
- new net DIG_4B11: IC12.14, U12.9
- new net DIG_4B12: IC13.14, U13.9
- new net DIG_4B13: IC14.14, U14.9
- new net DIG_4B14: IC15.14, U15.9
- new net DIG_4B15: IC16.14, U16.9
- new net DIG_4B16: IC17.14, U17.9
- new net DIG_4B17: IC18.14, U18.9
- new net DIG_4B18: IC19.14, U19.9
- new net DIG_4B19: IC20.14, U20.9
- new net DIG_4B20: IC21.14, U21.9
- new net DIG_4B21: IC22.14, U22.9
- new net DIG_4B22: IC23.14, U23.9
- new net DIG_4B23: IC24.14, U24.9
- new net DIG_4B24: IC25.14, U25.9
- new net DIG_4B9: IC10.14, U10.9
- new net DIG_DP10: IC11.13, U11.7
- new net DIG_DP11: IC12.13, U12.7
- new net DIG_DP12: IC13.13, U13.7
- new net DIG_DP13: IC14.13, U14.7
- new net DIG_DP14: IC15.13, U15.7
- new net DIG_DP15: IC16.13, U16.7
- new net DIG_DP16: IC17.13, U17.7
- new net DIG_DP17: IC18.13, U18.7
- new net DIG_DP18: IC19.13, U19.7
- new net DIG_DP19: IC20.13, U20.7
- new net DIG_DP20: IC21.13, U21.7
- new net DIG_DP21: IC22.13, U22.7
- new net DIG_DP22: IC23.13, U23.7
- new net DIG_DP23: IC24.13, U24.7
- new net DIG_DP24: IC25.13, U25.7
- new net DIG_DP9: IC10.13, U10.7
- new net GND10: C11.2, D21.C, IC11.1, J31.1, J32.1, J33.1
- new net GND11: C12.2, D23.C, IC12.1, J34.1, J35.1, J36.1
- new net GND12: C13.2, D25.C, IC13.1, J37.1, J38.1, J39.1
- new net GND13: C14.2, D27.C, IC14.1, J40.1, J41.1, J42.1
- new net GND14: C15.2, D29.C, IC15.1, J43.1, J44.1, J45.1
- new net GND15: C16.2, D31.C, IC16.1, J46.1, J47.1, J48.1
- new net GND16: C17.2, D33.C, IC17.1, J49.1, J50.1, J51.1
- new net GND17: C18.2, D35.C, IC18.1, J52.1, J53.1, J54.1
- new net GND18: C19.2, D37.C, IC19.1, J55.1, J56.1, J57.1
- new net GND19: C20.2, D39.C, IC20.1, J58.1, J59.1, J60.1
- new net GND20: C21.2, D41.C, IC21.1, J61.1, J62.1, J63.1
- new net GND21: C22.2, D43.C, IC22.1, J64.1, J65.1, J66.1
- new net GND22: C23.2, D45.C, IC23.1, J67.1, J68.1, J69.1
- new net GND23: C24.2, D47.C, IC24.1, J70.1, J71.1, J72.1
- new net GND24: C25.2, D49.C, IC25.1, J73.1, J74.1, J75.1
- new net GND9: C10.2, D19.C, IC10.1, J28.1, J29.1, J30.1
- new net N$100: I2C14.1, R73.2
- new net N$101: I2C14.3, R72.2
- new net N$102: JP29.2, R74.1
- new net N$103: JP30.2, R75.1
- new net N$104: D30.C, R74.2, R75.2
- new net N$105: 3V15.1, R71.2
- new net N$106: D31.A, R76.1
- new net N$107: I2C15.1, R78.2
- new net N$108: I2C15.3, R77.2
- new net N$109: JP31.2, R79.1
- new net N$110: JP32.2, R80.1
- new net N$111: D32.C, R79.2, R80.2
- new net N$112: 3V16.1, R76.2
- new net N$113: D33.A, R81.1
- new net N$114: I2C16.1, R83.2
- new net N$115: I2C16.3, R82.2
- new net N$116: JP33.2, R84.1
- new net N$117: JP34.2, R85.1
- new net N$118: D34.C, R84.2, R85.2
- new net N$119: 3V17.1, R81.2
- new net N$120: D35.A, R86.1
- new net N$121: I2C17.1, R88.2
- new net N$122: I2C17.3, R87.2
- new net N$123: JP35.2, R89.1
- new net N$124: JP36.2, R90.1
- new net N$125: D36.C, R89.2, R90.2
- new net N$126: 3V18.1, R86.2
- new net N$127: D37.A, R91.1
- new net N$128: I2C18.1, R93.2
- new net N$129: I2C18.3, R92.2
- new net N$130: JP37.2, R94.1
- new net N$131: JP38.2, R95.1
- new net N$132: D38.C, R94.2, R95.2
- new net N$133: 3V19.1, R91.2
- new net N$134: D39.A, R96.1
- new net N$135: I2C19.1, R98.2
- new net N$136: I2C19.3, R97.2
- new net N$137: JP39.2, R99.1
- new net N$138: JP40.2, R100.1
- new net N$139: D40.C, R100.2, R99.2
- new net N$140: 3V20.1, R96.2
- new net N$141: D41.A, R101.1
- new net N$142: I2C20.1, R103.2
- new net N$143: I2C20.3, R102.2
- new net N$144: JP41.2, R104.1
- new net N$145: JP42.2, R105.1
- new net N$146: D42.C, R104.2, R105.2
- new net N$147: 3V21.1, R101.2
- new net N$148: D43.A, R106.1
- new net N$149: I2C21.1, R108.2
- new net N$150: I2C21.3, R107.2
- new net N$151: JP43.2, R109.1
- new net N$152: JP44.2, R110.1
- new net N$153: D44.C, R109.2, R110.2
- new net N$154: 3V22.1, R106.2
- new net N$155: D45.A, R111.1
- new net N$156: I2C22.1, R113.2
- new net N$157: I2C22.3, R112.2
- new net N$158: JP45.2, R114.1
- new net N$159: JP46.2, R115.1
- new net N$160: D46.C, R114.2, R115.2
- new net N$161: 3V23.1, R111.2
- new net N$162: D47.A, R116.1
- new net N$163: I2C23.1, R118.2
- new net N$164: I2C23.3, R117.2
- new net N$165: JP47.2, R119.1
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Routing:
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- added copper zone on layer 1, net GND10
- added copper zone on layer 16, net GND10
- added copper zone on layer 1, net GND11
- added copper zone on layer 16, net GND11
- added copper zone on layer 1, net GND12
- added copper zone on layer 16, net GND12
- added copper zone on layer 1, net GND13
- added copper zone on layer 16, net GND13
- added copper zone on layer 1, net GND14
- added copper zone on layer 16, net GND14
- added copper zone on layer 1, net GND15
- added copper zone on layer 16, net GND15
- added copper zone on layer 1, net GND16
- added copper zone on layer 16, net GND16
- added copper zone on layer 1, net GND17
- added copper zone on layer 16, net GND17
- added copper zone on layer 1, net GND18
- added copper zone on layer 16, net GND18
- added copper zone on layer 1, net GND19
- added copper zone on layer 16, net GND19
- added copper zone on layer 1, net GND20
- added copper zone on layer 16, net GND20
- added copper zone on layer 1, net GND21
- added copper zone on layer 16, net GND21
- added copper zone on layer 1, net GND22
- added copper zone on layer 16, net GND22
- added copper zone on layer 1, net GND23
- added copper zone on layer 16, net GND23
- added copper zone on layer 1, net GND24
- added copper zone on layer 16, net GND24
- added copper zone on layer 1, net GND9
- added copper zone on layer 16, net GND9
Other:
- board size 143 x 112.5 mm -> 240.5 x 155.4 mm
- board text added: "Route Out"
